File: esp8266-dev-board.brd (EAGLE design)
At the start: 25.4 x 33 mm, 9 parts

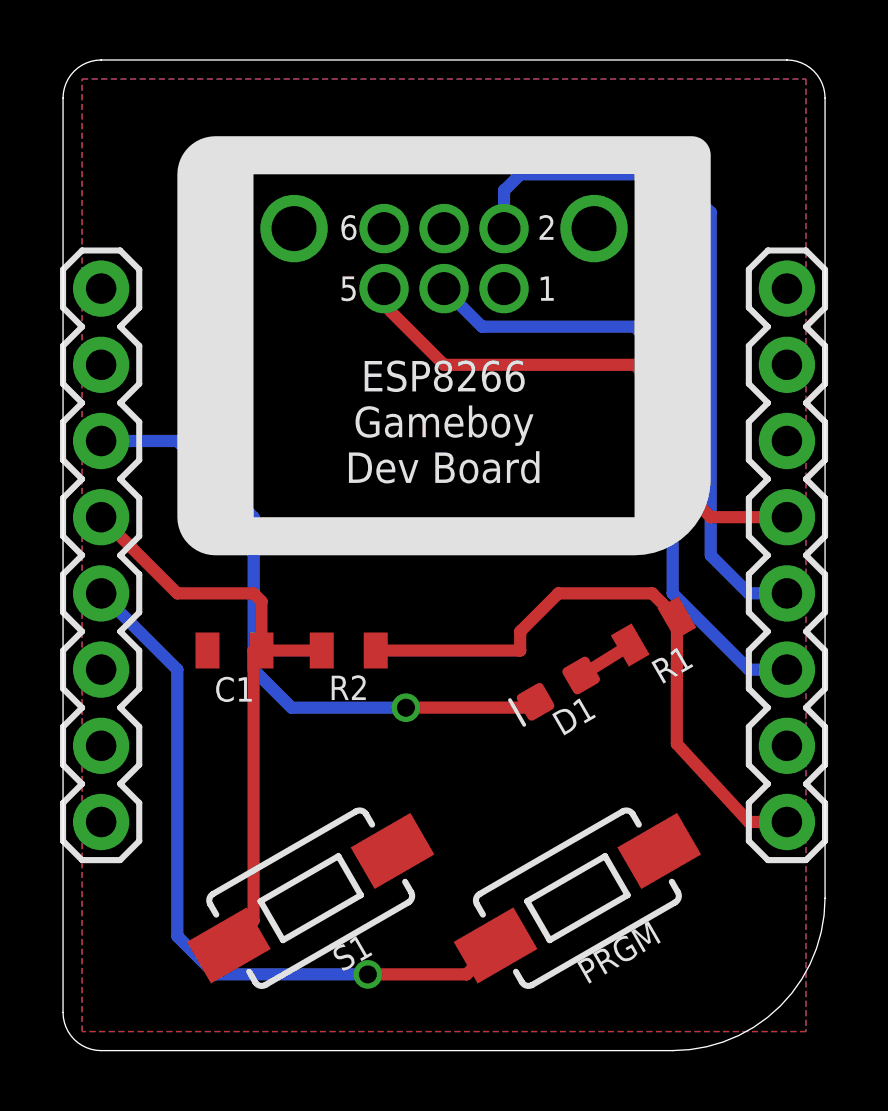
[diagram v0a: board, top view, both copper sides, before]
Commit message: Fix dimensions
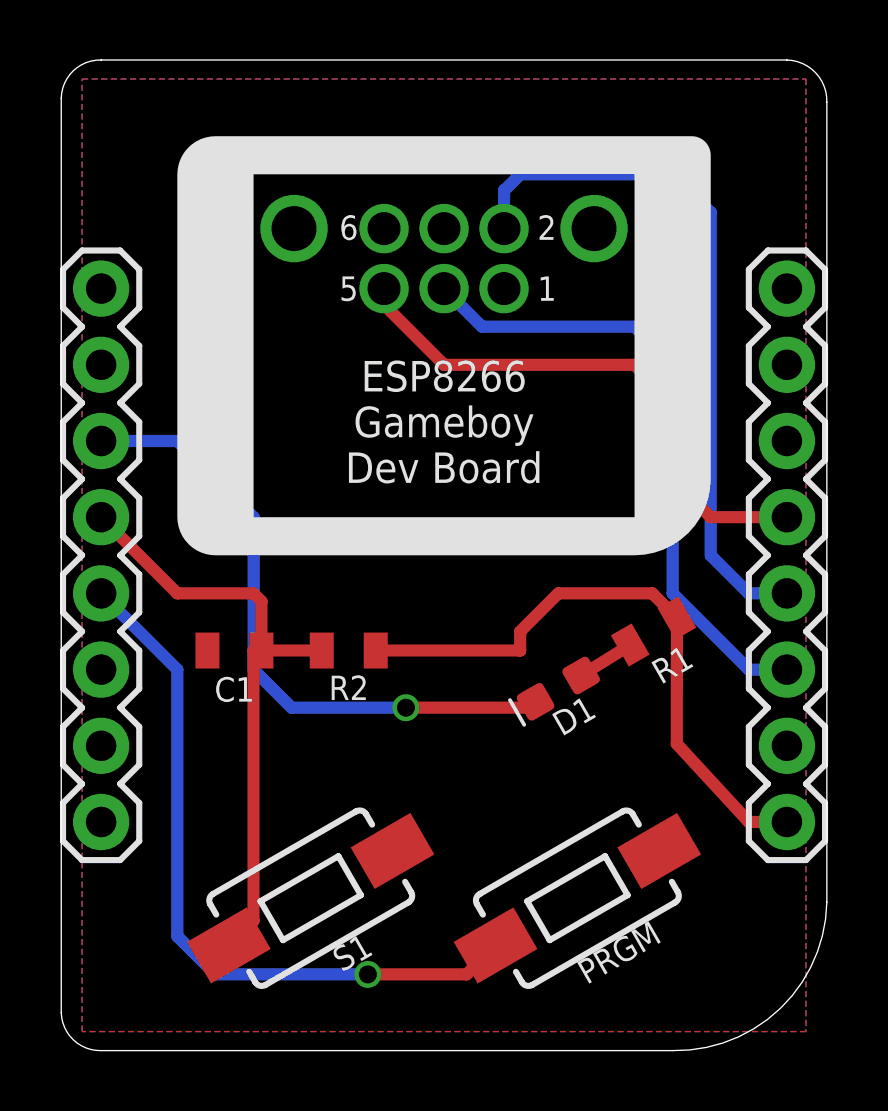
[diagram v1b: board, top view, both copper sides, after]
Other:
- board size 25.4 x 33 mm -> 25.5 x 33 mm
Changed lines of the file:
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@@
 <?xml version="1.0" encoding="utf-8"?>
 <!DOCTYPE eagle SYSTEM "eagle.dtd">
-<eagle version="7.3.0">
+<eagle version="9.2.2">
 <drawing>
 <settings>
 <setting alwaysvectorfont="no"/>
+<setting keepoldvectorfont="yes"/>
 <setting verticaltext="up"/>
 </settings>
-<grid distance="0.05" unitdist="inch" unit="mm" style="lines" multiple="1" display="yes" altdistance="0.025" altunitdist="inch" altunit="mm"/>
+<grid distance="0.01" unitdist="mm" unit="mm" style="lines" multiple="1" display="yes" altdistance="0.025" altunitdist="inch" altunit="mm"/>
 <layers>
 <layer number="1" name="Top" color="4" fill="1" visible="yes" active="yes"/>
@@
 <plain>
 <wire x1="0" y1="-1.27" x2="19.05" y2="-1.27" width="0" layer="20"/>
-<wire x1="24.13" y1="3.81" x2="24.13" y2="30.48" width="0" layer="20"/>
+<wire x1="24.19" y1="3.68" x2="24.19" y2="30.35" width="0" layer="20"/>
 <wire x1="22.86" y1="31.75" x2="0" y2="31.75" width="0" layer="20"/>
-<wire x1="-1.27" y1="30.48" x2="-1.27" y2="0" width="0" layer="20"/>
-<wire x1="24.13" y1="3.81" x2="19.05" y2="-1.27" width="0" layer="20" curve="-90"/>
-<wire x1="0" y1="31.75" x2="-1.27" y2="30.48" width="0" layer="20" curve="90"/>
-<wire x1="24.13" y1="30.48" x2="22.86" y2="31.75" width="0" layer="20" curve="90"/>
-<wire x1="-1.27" y1="0" x2="0" y2="-1.27" width="0" layer="20" curve="90"/>
+<wire x1="-1.33" y1="30.48" x2="-1.33" y2="0" width="0" layer="20"/>
+<wire x1="24.19" y1="3.68" x2="19.05" y2="-1.27" width="0" layer="20" curve="-90"/>
+<wire x1="0" y1="31.75" x2="-1.33" y2="30.48" width="0" layer="20" curve="90"/>
+<wire x1="24.19" y1="30.35" x2="22.86" y2="31.75" width="0" layer="20" curve="90"/>
+<wire x1="-1.33" y1="0" x2="0" y2="-1.27" width="0" layer="20" curve="90"/>
 <polygon width="0" layer="21">
 <vertex x="17.78" y="29.21"/>
@@
 </classes>
 <designrules name="oshpark-2layer">
-<description language="de">&lt;b&gt;EAGLE Design Rules&lt;/b&gt;
+<description language="en">&lt;b&gt;OSH Park Design Rules&lt;/b&gt;
 &lt;p&gt;
-Die Standard-Design-Rules sind so gewählt, dass sie für
-die meisten Anwendungen passen. Sollte ihre Platine
-besondere Anforderungen haben, treffen Sie die erforderlichen
-Einstellungen hier und speichern die Design Rules unter
-einem neuen Namen ab.</description>
-<description language="en">&lt;b&gt;Laen's PCB Order Design Rules&lt;/b&gt;
+Please make sure your boards conform to these design rules.
+&lt;/p&gt;
 &lt;p&gt;
-Please make sure your boards conform to these design rules.</description>
+Note, that not all DRC settings must be set by the manufacturer. Several can be adjusted for the design, including those listed on our docs page here.
+&lt;a href=&quot;http://docs.oshpark.com/design-tools/eagle/design-rules-files/&quot;&gt;Adjustable Settings&lt;/a&gt;
+&lt;/p&gt;</description>
 <param name="layerSetup" value="(1*16)"/>
-<param name="mtCopper" value="0.0356mm 0.0356mm 0.0356mm 0.0356mm 0.0356mm 0.0356mm 0.0356mm 0.0356mm 0.0356mm 0.0356mm 0.0356mm 0.0356mm 0.0356mm 0.0356mm 0.0356mm 0.0356mm"/>
-<param name="mtIsolate" value="1.5011mm 0.1499mm 0.2007mm 0.1499mm 0.2007mm 0.1499mm 0.2007mm 0.1499mm 0.2007mm 0.1499mm 0.2007mm 0.1499mm 0.2007mm 0.1499mm 0.2007mm"/>
+<param name="mtCopper" value="0.035559375mm 0.0356mm 0.0356mm 0.0356mm 0.0356mm 0.0356mm 0.0356mm 0.0356mm 0.0356mm 0.0356mm 0.0356mm 0.0356mm 0.0356mm 0.0356mm 0.0356mm 0.035559375mm"/>
+<param name="mtIsolate" value="1.6mm 0.1499mm 0.2007mm 0.1499mm 0.2007mm 0.1499mm 0.2007mm 0.1499mm 0.2007mm 0.1499mm 0.2007mm 0.1499mm 0.2007mm 0.1499mm 0.2007mm"/>
 <param name="mdWireWire" value="6mil"/>
 <param name="mdWirePad" value="6mil"/>
@@
 <param name="mdSmdStop" value="0mil"/>
 <param name="msWidth" value="6mil"/>
-<param name="msDrill" value="13mil"/>
-<param name="msMicroVia" value="13mil"/>
+<param name="msDrill" value="10mil"/>
+<param name="msMicroVia" value="10mil"/>
 <param name="msBlindViaRatio" value="0.5"/>
 <param name="rvPadTop" value="0.25"/>
@@
 <param name="rvMicroViaOuter" value="0.25"/>
 <param name="rvMicroViaInner" value="0.25"/>
-<param name="rlMinPadTop" value="7mil"/>
+<param name="rlMinPadTop" value="5mil"/>
 <param name="rlMaxPadTop" value="20mil"/>
-<param name="rlMinPadInner" value="7mil"/>
+<param name="rlMinPadInner" value="5mil"/>
 <param name="rlMaxPadInner" value="20mil"/>
-<param name="rlMinPadBottom" value="7mil"/>
+<param name="rlMinPadBottom" value="5mil"/>
 <param name="rlMaxPadBottom" value="20mil"/>
-<param name="rlMinViaOuter" value="7mil"/>
+<param name="rlMinViaOuter" value="5mil"/>
 <param name="rlMaxViaOuter" value="20mil"/>
-<param name="rlMinViaInner" value="7mil"/>
+<param name="rlMinViaInner" value="5mil"/>
 <param name="rlMaxViaInner" value="20mil"/>
-<param name="rlMinMicroViaOuter" value="4mil"/>
+<param name="rlMinMicroViaOuter" value="5mil"/>
 <param name="rlMaxMicroViaOuter" value="20mil"/>
-<param name="rlMinMicroViaInner" value="4mil"/>
+<param name="rlMinMicroViaInner" value="5mil"/>
 <param name="rlMaxMicroViaInner" value="20mil"/>
 <param name="psTop" value="-1"/>
@@
 <param name="dpMaxLengthDifference" value="10mm"/>
 <param name="dpGapFactor" value="2.5"/>
-<param name="checkGrid" value="0"/>
 <param name="checkAngle" value="0"/>
 <param name="checkFont" value="1"/>
 <param name="checkRestrict" value="1"/>
+<param name="checkStop" value="0"/>
+<param name="checkValues" value="0"/>
+<param name="checkNames" value="1"/>
+<param name="checkWireStubs" value="1"/>
+<param name="checkPolygonWidth" value="0"/>
 <param name="useDiameter" value="13"/>
 <param name="maxErrors" value="50"/>
@@
 </element>
 <element name="S1" library="SparkFun-Switches" package="TACTILE_SWITCH_SMD_6.0X3.5MM" value="" x="6.985" y="3.81" smashed="yes" rot="R30">
+<attribute name="NAME" x="8.5725" y="1.649778125" size="0.8128" layer="25" font="vector" ratio="20" rot="R30" align="bottom-center"/>
 <attribute name="PROD_ID" value="SWCH-00815" x="6.985" y="3.81" size="1.778" layer="27" rot="R30" display="off"/>
 <attribute name="SF_SKU" value="COM-08229" x="6.985" y="3.81" size="1.778" layer="27" rot="R30" display="off"/>
-<attribute name="NAME" x="8.5725" y="1.649778125" size="0.8128" layer="25" font="vector" ratio="20" rot="R30" align="bottom-center"/>
 <attribute name="VALUE" x="7.9375" y="2.16021875" size="0.6096" layer="27" font="vector" ratio="20" rot="R30" align="top-center"/>
 </element>
 <element name="PRGM" library="SparkFun-Switches" package="TACTILE_SWITCH_SMD_6.0X3.5MM" value="" x="15.875" y="3.81" smashed="yes" rot="R30">
+<attribute name="NAME" x="17.4625" y="1.649778125" size="0.8128" layer="25" font="vector" ratio="20" rot="R30" align="bottom-center"/>
 <attribute name="PROD_ID" value="SWCH-00815" x="15.875" y="3.81" size="1.778" layer="27" rot="R30" display="off"/>
 <attribute name="SF_SKU" value="COM-08229" x="15.875" y="3.81" size="1.778" layer="27" rot="R30" display="off"/>
-<attribute name="NAME" x="17.4625" y="1.649778125" size="0.8128" layer="25" font="vector" ratio="20" rot="R30" align="bottom-center"/>
 <attribute name="VALUE" x="16.8275" y="2.16021875" size="0.6096" layer="27" font="vector" ratio="20" rot="R30" align="top-center"/>
 </element>
-<element name="U$1" library="arcadetv" package="EXT-PORT-AGB" value="EXT-PORT-AGB" x="11.43" y="24.13" rot="MR0"/>
+<element name="U$1" library="arcadetv" package="EXT-PORT-AGB" value="EXT-PORT-AGB" x="11.43" y="24.13" smashed="yes" rot="MR0"/>
 <element name="D1" library="SparkFun-LED" package="LED-0603" value="" x="15.24" y="10.795" smashed="yes" rot="R210">
 <attribute name="NAME" x="15.5575" y="10.245071875" size="0.8128" layer="25" font="vector" ratio="20" rot="R210" align="bottom-center"/>
@@
 </element>
 <element name="R1" library="SparkFun-Resistors" package="0805" value=" " x="18.415" y="12.7" smashed="yes" rot="R30">
+<attribute name="NAME" x="19.2405" y="11.24739375" size="0.8128" layer="25" font="vector" ratio="20" rot="R30" align="bottom-center"/>
 <attribute name="PROD_ID" value=" " x="18.415" y="12.7" size="1.778" layer="27" rot="R30" display="off"/>
-<attribute name="NAME" x="19.2405" y="11.24739375" size="0.8128" layer="25" font="vector" ratio="20" rot="R30" align="bottom-center"/>
 </element>
 <element name="R2" library="SparkFun-Resistors" package="0805" value=" " x="8.255" y="12.065" smashed="yes">
+<attribute name="NAME" x="8.255" y="10.414" size="0.8128" layer="25" font="vector" ratio="20" align="bottom-center"/>
 <attribute name="PROD_ID" value=" " x="8.255" y="12.065" size="1.778" layer="27" display="off"/>
-<attribute name="NAME" x="8.255" y="10.414" size="0.8128" layer="25" font="vector" ratio="20" align="bottom-center"/>
 <attribute name="VALUE" x="8.255" y="11.176" size="0.6096" layer="27" font="vector" ratio="20" align="top-center"/>
 </element>
 <element name="C1" library="SparkFun-Capacitors" package="0805" value="10uF" x="4.445" y="12.065" smashed="yes" rot="R180">
+<attribute name="NAME" x="4.445" y="11.176" size="0.8128" layer="25" font="vector" ratio="20" rot="R180" align="bottom-center"/>
 <attribute name="PROD_ID" value="CAP-11330" x="4.445" y="12.065" size="1.778" layer="27" rot="R180" display="off"/>
-<attribute name="NAME" x="4.445" y="11.176" size="0.8128" layer="25" font="vector" ratio="20" rot="R180" align="bottom-center"/>
 </element>
 </elements>
@@
 <contactref element="S1" pad="1"/>
 <contactref element="C1" pad="1"/>
-<wire x1="4.075" y1="2.41701875" x2="4.25701875" y2="2.235" width="0.4064" layer="1"/>
 <wire x1="0" y1="16.51" x2="2.54" y2="13.97" width="0.4064" layer="1"/>
 <wire x1="2.54" y1="13.97" x2="5.08" y2="13.97" width="0.4064" layer="1"/>
@@
 </signal>
 </signals>
+<mfgpreviewcolors>
+<mfgpreviewcolor name="soldermaskcolor" color="0xC8008000"/>
+<mfgpreviewcolor name="silkscreencolor" color="0xFFFEFEFE"/>
+<mfgpreviewcolor name="backgroundcolor" color="0xFF282828"/>
+<mfgpreviewcolor name="coppercolor" color="0xFFFFBF00"/>
+<mfgpreviewcolor name="substratecolor" color="0xFF786E46"/>
+</mfgpreviewcolors>
 </board>
 </drawing>

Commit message: Fix sch warnings
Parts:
- D1: value (none) -> red
- J1: value (none) -> left
- J2: value (none) -> right
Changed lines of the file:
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@@
 </class>
 </classes>
-<designrules name="oshpark-2layer">
+<designrules name="oshpark-2layer *">
 <description language="en">&lt;b&gt;OSH Park Design Rules&lt;/b&gt;
 &lt;p&gt;
@@
 <param name="checkRestrict" value="1"/>
 <param name="checkStop" value="0"/>
-<param name="checkValues" value="0"/>
+<param name="checkValues" value="1"/>
 <param name="checkNames" value="1"/>
 <param name="checkWireStubs" value="1"/>
-<param name="checkPolygonWidth" value="0"/>
+<param name="checkPolygonWidth" value="1"/>
 <param name="useDiameter" value="13"/>
 <param name="maxErrors" value="50"/>
@@
 </autorouter>
 <elements>
-<element name="J1" library="SparkFun-Connectors" package="1X08_ROUND" value="" x="0" y="6.35" smashed="yes" rot="R90">
+<element name="J1" library="SparkFun-Connectors" package="1X08_ROUND" value="left" x="0" y="6.35" smashed="yes" rot="R90">
 <attribute name="PROD_ID" value="CONN-08437" x="0" y="6.35" size="1.778" layer="27" rot="R90" display="off"/>
 <attribute name="VALUE" x="3.175" y="5.08" size="1.27" layer="27" rot="R90"/>
 </element>
-<element name="J2" library="SparkFun-Connectors" package="1X08_ROUND" value="" x="22.86" y="6.35" smashed="yes" rot="R90">
+<element name="J2" library="SparkFun-Connectors" package="1X08_ROUND" value="right" x="22.86" y="6.35" smashed="yes" rot="R90">
 <attribute name="PROD_ID" value="CONN-08437" x="22.86" y="6.35" size="1.778" layer="27" rot="R90" display="off"/>
 <attribute name="VALUE" x="26.035" y="5.08" size="1.27" layer="27" rot="R90"/>
@@
 </element>
 <element name="U$1" library="arcadetv" package="EXT-PORT-AGB" value="EXT-PORT-AGB" x="11.43" y="24.13" smashed="yes" rot="MR0"/>
-<element name="D1" library="SparkFun-LED" package="LED-0603" value="" x="15.24" y="10.795" smashed="yes" rot="R210">
+<element name="D1" library="SparkFun-LED" package="LED-0603" value="red" x="15.24" y="10.795" smashed="yes" rot="R210">
 <attribute name="NAME" x="15.5575" y="10.245071875" size="0.8128" layer="25" font="vector" ratio="20" rot="R210" align="bottom-center"/>
 <attribute name="VALUE" x="14.9225" y="11.344925" size="0.6096" layer="27" font="vector" ratio="20" rot="R210" align="top-center"/>

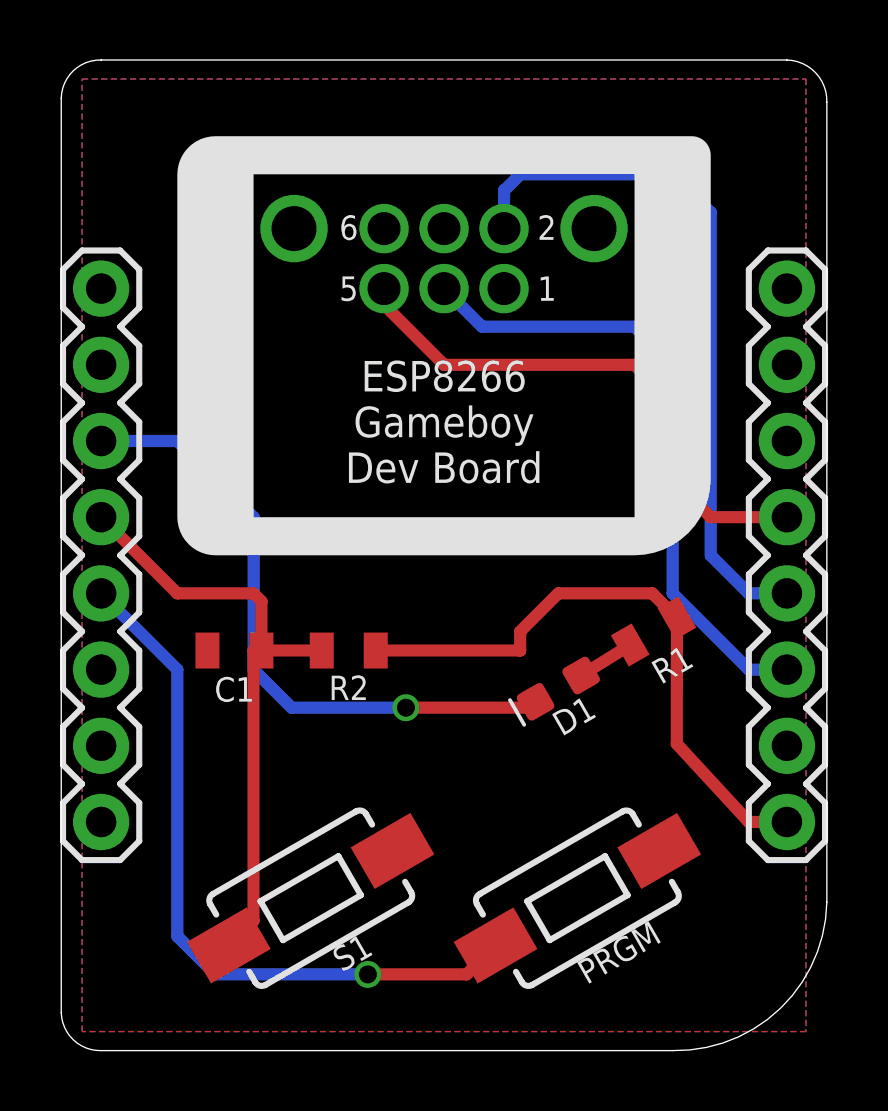
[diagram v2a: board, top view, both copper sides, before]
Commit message: Fixed zero width polygons and top silkscreen
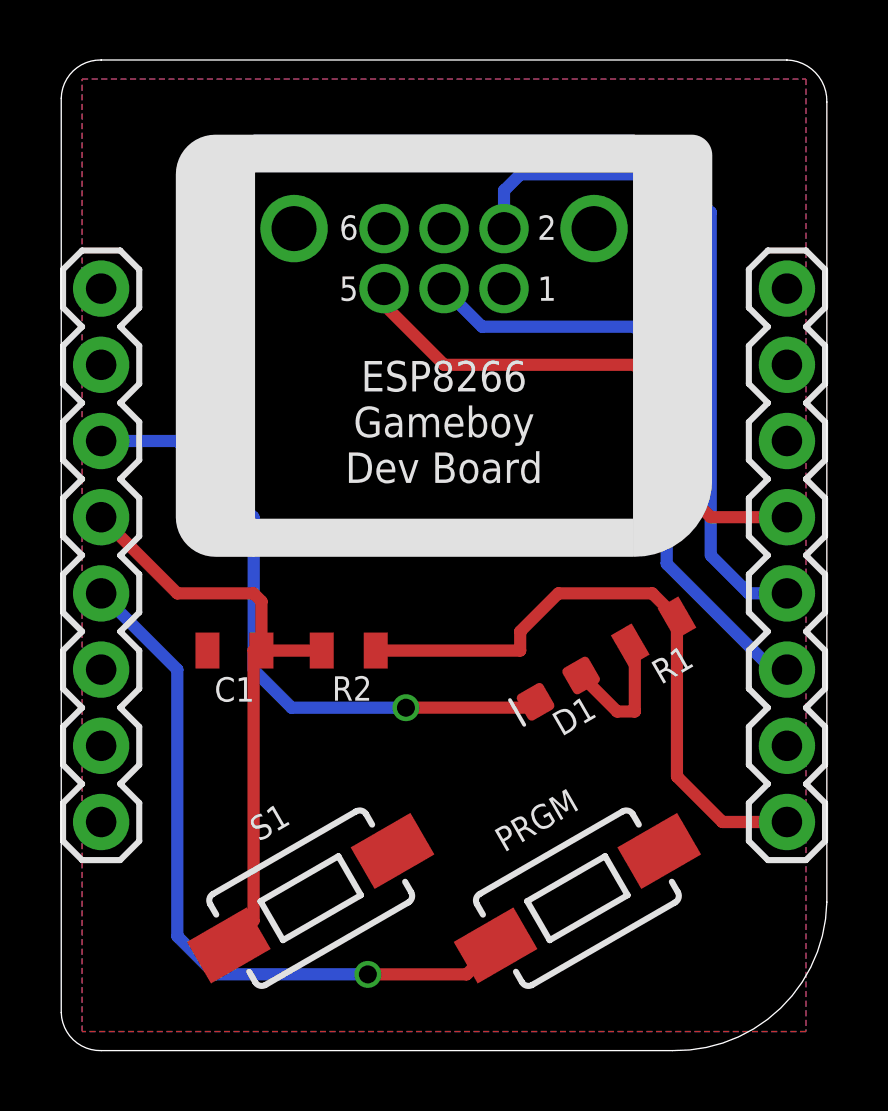
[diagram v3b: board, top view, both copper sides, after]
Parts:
- R1, R2: value (none) -> 4.7k
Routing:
- net N$4: track 1.93 -> 4.57 mm
- net VCC: track 20.5 -> 21.1 mm
